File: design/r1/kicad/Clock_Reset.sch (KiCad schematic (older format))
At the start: 31 parts, among them IC7 7404N, IC8 555N, IC9 74LS01N, Q2 8MHz

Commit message: Initial cleanup
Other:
- note added: "1"
- note added: "CLOCK & RESET"
- note added: "Copyright ©2019-2020 Ross Bamford and Contributors.\nOpen Source Hardware licenced under CERN Open Hardware Licence. \nSee https://github.com/roscopeco/rosco_m68k/blob/master/LICENCE.hardware.txt\nOSHWA UK000006 (https://certification.oshwa.org/uk000006.html)\n"
- note removed: "2020-02-25\nPersonally I would add an Inductor or ferrite core right after the power\nconnector. (And use a bigger connector with screw terminals)."
- note removed: "2020-02-25\nThese "PWR_FLAG" symbols are to indicate that these wires are "Power" connections.\nIC normally have Power inputs, and ERC will generate errors if any of\n the "power connections" of a component is not connected to these\n "PWR_FLAG" symbols."
- note removed: "2020-02-25\nThese 2 Vcc and GND symbols are from KiCad's own library.\nThese symbols have internal Vcc and GND labels, and\nif you use these throughout your schematic, you can omit the Vcc\nand GND labels generated by the Eagle -> KiCad conversion."
- note removed: "2020-02-25\nWhat sort of weird oscillator is this?\nNormally there is an inverting amplifier across the Xtal."
- note removed: "CLOCK\n& RESET"
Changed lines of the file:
@@
-$EndComp
-$Comp
-L rosco_m68k-eagle-import:A3L-LOC #FRAME4
-U 1 1 16F02BA1
-P 1100 10300
-AR Path="/16F02BA1" Ref="#FRAME4"  Part="1"
-AR Path="/5E53B952/16F02BA1" Ref="#FRAME4"  Part="1"
-F 0 "#FRAME4" H 1100 10300 50  0001 C CNN
-F 1 "BOOT line generator" H 1100 10300 50  0001 C CNN
-F 2 "" H 1100 10300 50  0001 C CNN
-F 3 "" H 1100 10300 50  0001 C CNN
-	1    1100 10300
-	1    0    0    -1
 $EndComp
 $Comp
@@
 Text Notes 3600 4500 0    59   ~ 0
 SYSTEM CLOCK CIRCUIT
-Text Notes 12900 10000 0    170  ~ 0
-CLOCK\n& RESET
 NoConn ~ 9000 7900
 NoConn ~ 8600 7900
 NoConn ~ 9500 6400
-Wire Bus Line
-	2300 8300 4600 8300
 $Comp
 L power:PWR_FLAG #FLG0101
@@
 	1    0    0    -1
 $EndComp
-Text Notes 5850 2950 0    85   ~ 0
-2020-02-25\nWhat sort of weird oscillator is this?\nNormally there is an inverting amplifier across the Xtal.
-Text Notes 11700 3350 0    75   ~ 0
-2020-02-25\nThese "PWR_FLAG" symbols are to indicate that these wires are "Power" connections.\nIC normally have Power inputs, and ERC will generate errors if any of\n the "power connections" of a component is not connected to these\n "PWR_FLAG" symbols.
-Text Notes 10200 1900 0    50   ~ 0
-2020-02-25\nThese 2 Vcc and GND symbols are from KiCad's own library.\nThese symbols have internal Vcc and GND labels, and\nif you use these throughout your schematic, you can omit the Vcc\nand GND labels generated by the Eagle -> KiCad conversion.
-Text Notes 14950 1800 0    50   ~ 0
-2020-02-25\nPersonally I would add an Inductor or ferrite core right after the power\nconnector. (And use a bigger connector with screw terminals).
+Text Notes 19300 10400 0    59   ~ 0
+CLOCK & RESET
+Text Notes 22550 10550 0    59   ~ 0
+1
+Text Notes 18950 9850 0    59   ~ 0
+Copyright ©2019-2020 Ross Bamford and Contributors.\nOpen Source Hardware licenced under CERN Open Hardware Licence. \nSee https://github.com/roscopeco/rosco_m68k/blob/master/LICENCE.hardware.txt\nOSHWA UK000006 (https://certification.oshwa.org/uk000006.html)\n
+Wire Bus Line
+	2300 8300 4600 8300
 $EndSCHEMATC

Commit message: Cleanup first pass
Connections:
- net /HALT renamed HALT
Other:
- moved on the sheet: C20, C21, C22, C23, C24, C25, C26, C27, C28, IC7A, IC7B, IC7C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

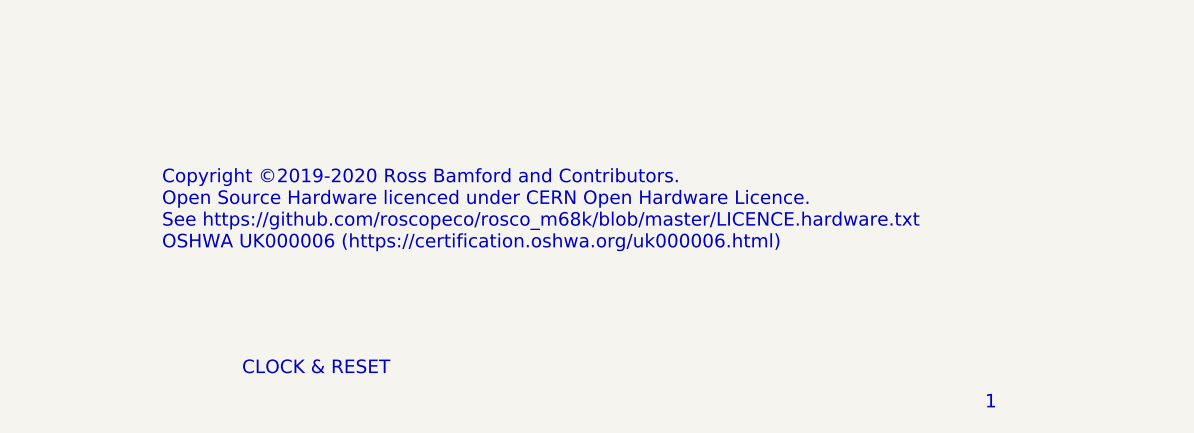
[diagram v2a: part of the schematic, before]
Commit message: Fix #18 and apply suggestions from #17
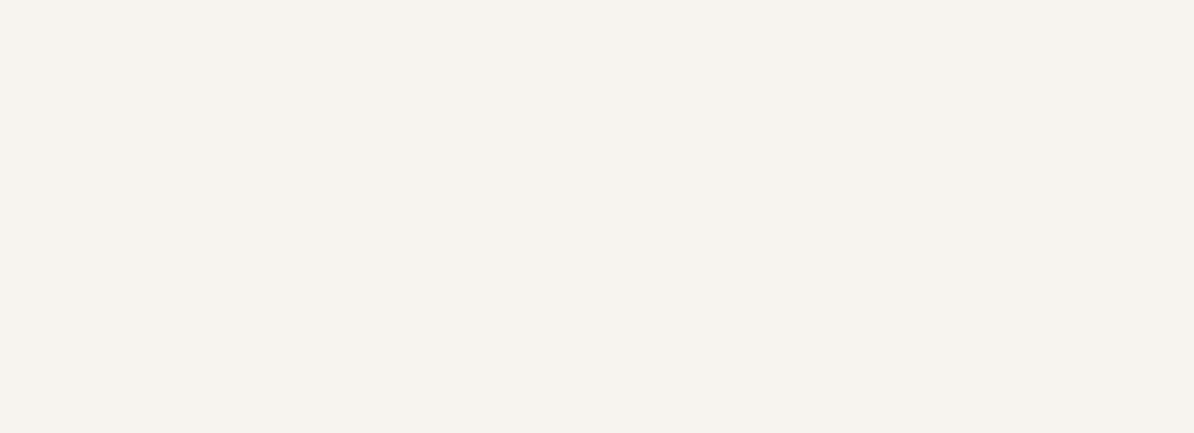
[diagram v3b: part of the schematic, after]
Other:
- note removed: "1"
- note removed: "CLOCK & RESET"
- note removed: "Copyright ©2019-2020 Ross Bamford and Contributors.\nOpen Source Hardware licenced under CERN Open Hardware Licence. \nSee https://github.com/roscopeco/rosco_m68k/blob/master/LICENCE.hardware.txt\nOSHWA UK000006 (https://certification.oshwa.org/uk000006.html)\n"
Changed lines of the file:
@@
 encoding utf-8
 Sheet 5 6
-Title ""
+Title "SYSTEM CLOCK AND RESET"
 Date "2020-02-25"
-Rev ""
+Rev "1"
 Comp ""
-Comment1 ""
-Comment2 ""
-Comment3 ""
-Comment4 ""
+Comment1 "OSHWA UK000006 (https://certification.oshwa.org/uk000006.html)"
+Comment2 "See https://github.com/roscopeco/rosco_m68k/blob/master/LICENCE.hardware.txt"
+Comment3 "Open Source Hardware licenced under CERN Open Hardware Licence"
+Comment4 "Copyright 2019-2020 Ross Bamford and Contributors"
 $EndDescr
 Wire Wire Line
@@
 	1    0    0    -1
 $EndComp
-Text Notes 19300 10400 0    59   ~ 0
-CLOCK & RESET
-Text Notes 22550 10550 0    59   ~ 0
-1
-Text Notes 18950 9850 0    59   ~ 0
-Copyright ©2019-2020 Ross Bamford and Contributors.\nOpen Source Hardware licenced under CERN Open Hardware Licence. \nSee https://github.com/roscopeco/rosco_m68k/blob/master/LICENCE.hardware.txt\nOSHWA UK000006 (https://certification.oshwa.org/uk000006.html)\n
 $Comp
 L power:GND #PWR0137

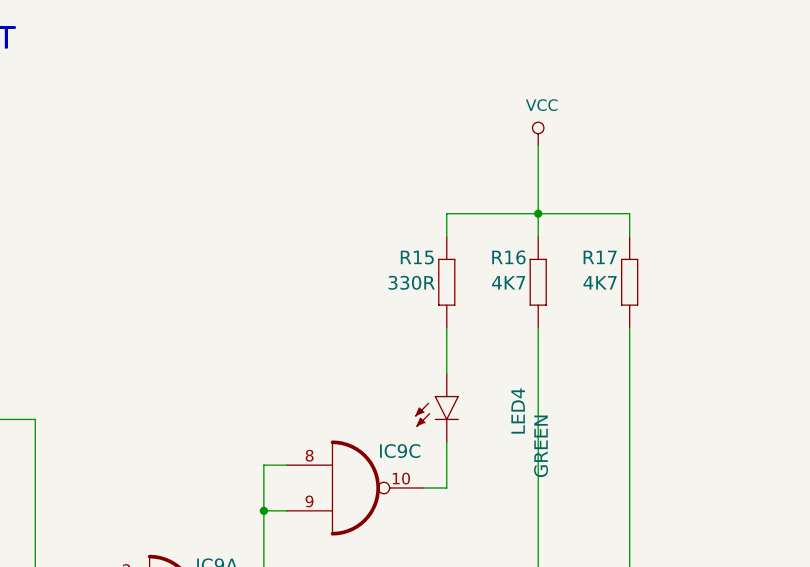
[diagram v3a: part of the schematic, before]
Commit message: Fix limiting resistors on R2 and R15
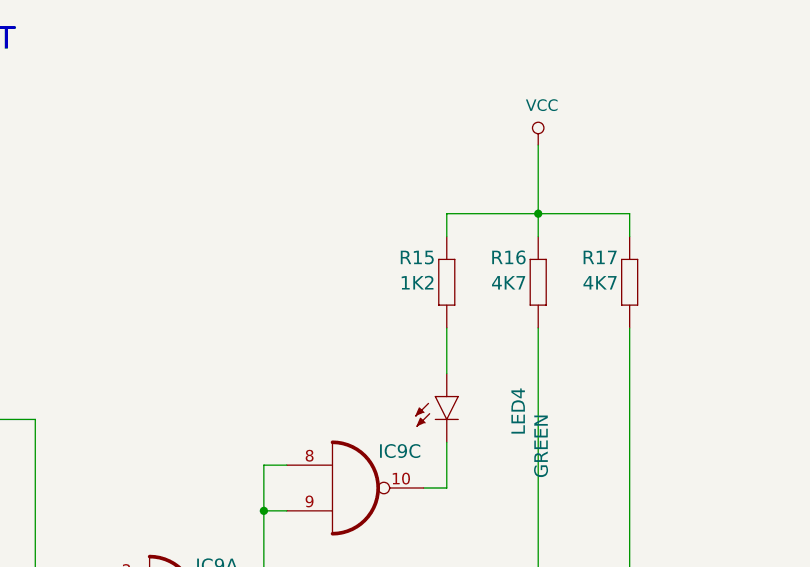
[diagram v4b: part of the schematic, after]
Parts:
- R15: value 330R -> 1K2
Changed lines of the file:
@@
 AR Path="/5E53B952/FD2CBBBB" Ref="R15"  Part="1"
 F 0 "R15" V 19941 5600 59  0000 L BNN
-F 1 "330R" V 19830 5600 59  0000 L BNN
+F 1 "1K2" V 19830 5600 59  0000 L BNN
 F 2 "rosco_m68k:0207_10" H 19800 5550 50  0001 C CNN
 F 3 "" H 19800 5550 50  0001 C CNN

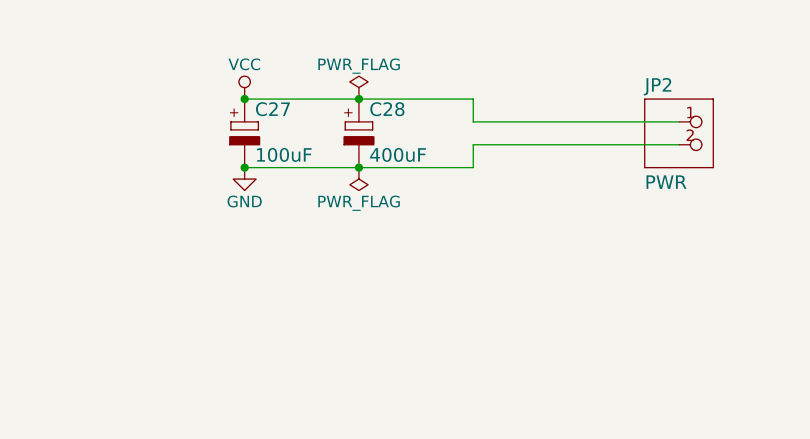
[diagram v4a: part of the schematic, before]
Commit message: Rerate current-limiting resistor for new green LEDs
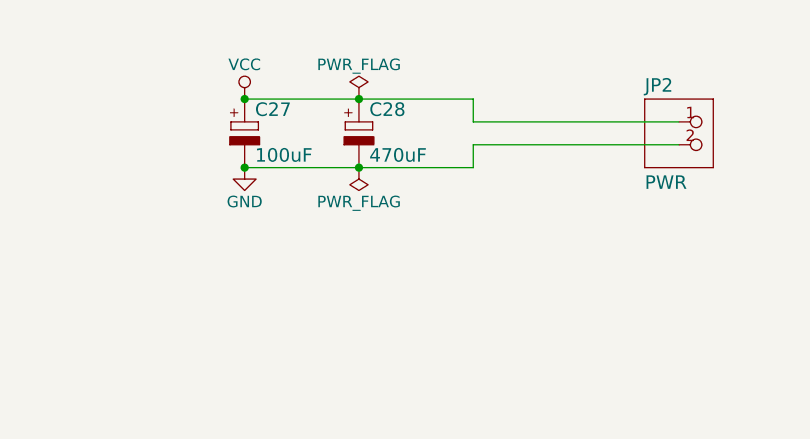
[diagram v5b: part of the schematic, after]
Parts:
- C28: value 400uF -> 470uF
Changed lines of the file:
@@
 AR Path="/5E53B952/FBED0E41" Ref="C28"  Part="1"
 F 0 "C28" H 15445 2319 59  0000 L BNN
-F 1 "400uF" H 15445 2119 59  0000 L BNN
+F 1 "470uF" H 15445 2119 59  0000 L BNN
 F 2 "rosco_m68k:E3,5-10" H 15400 2300 50  0001 C CNN
 F 3 "" H 15400 2300 50  0001 C CNN
